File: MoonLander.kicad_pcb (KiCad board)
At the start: 2 copper layers, 37.8 x 22.7 mm, 46 parts, among them IC1 MCP73831/2, IC2 BU33SD5, IC3 PRTR5V0U2X, IC4 CP2110-GM, IC5 LPC824M201JHI33, J1 Cortex_JTAG/SWD_10, P1 CONN_01X02, P2 CONN_01X02, P3 USB_OTG, P4 CONN_02X08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

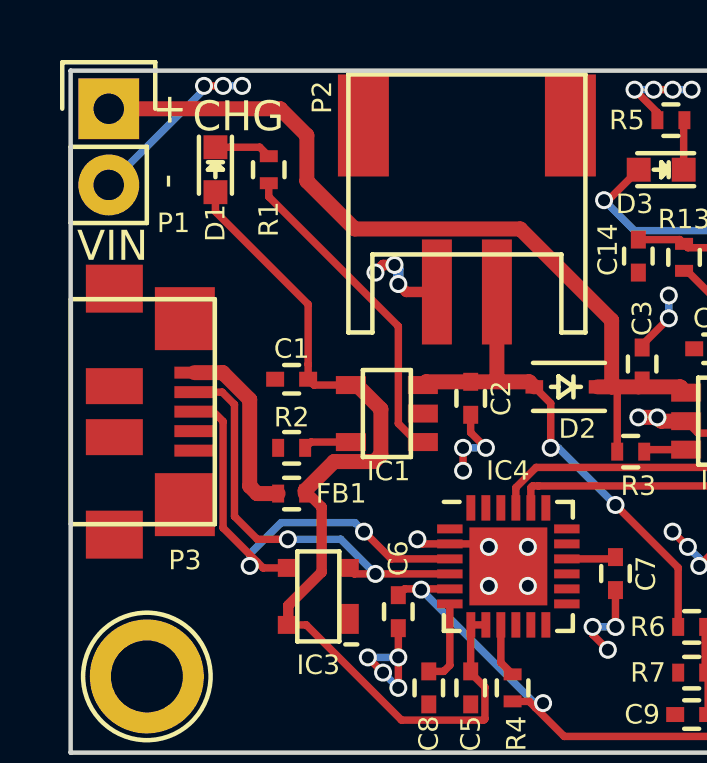
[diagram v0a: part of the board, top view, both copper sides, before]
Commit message: fixed reversed USB pinout
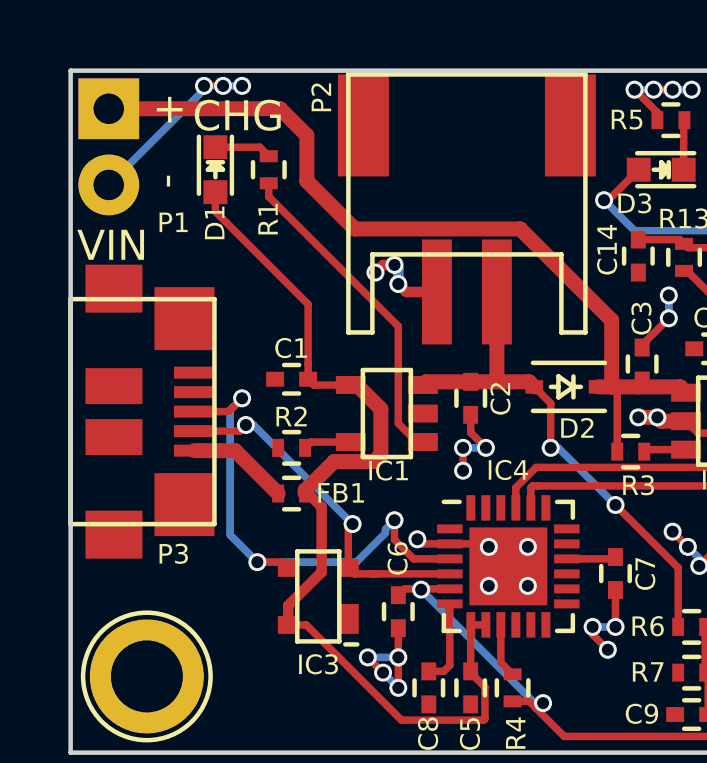
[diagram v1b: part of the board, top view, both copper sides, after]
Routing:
- net Net-(FB1-Pad2): track 6.15 -> 3.39 mm
- net /USB-Serial/USB_D-: track 14.2 -> 11.7 mm
- net /USB-Serial/USB_D+: track 15.7 -> 16.9 mm, vias 2 -> 3

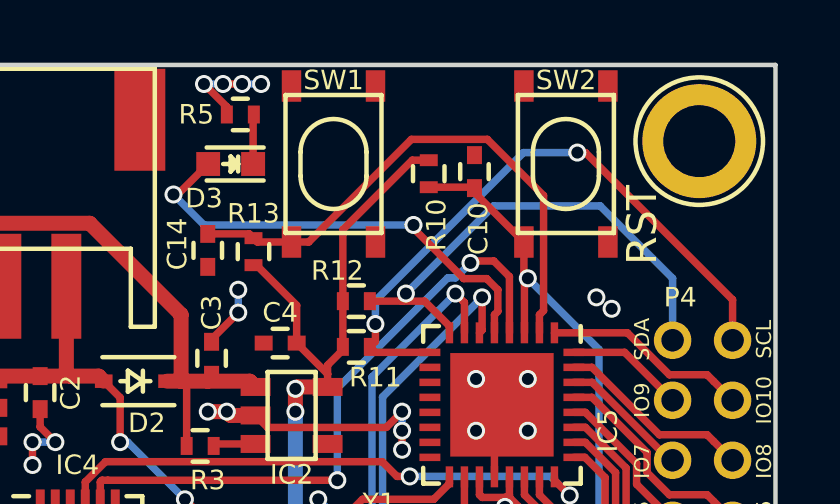
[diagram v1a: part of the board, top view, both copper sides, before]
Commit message: fixed switch footprint and pinout
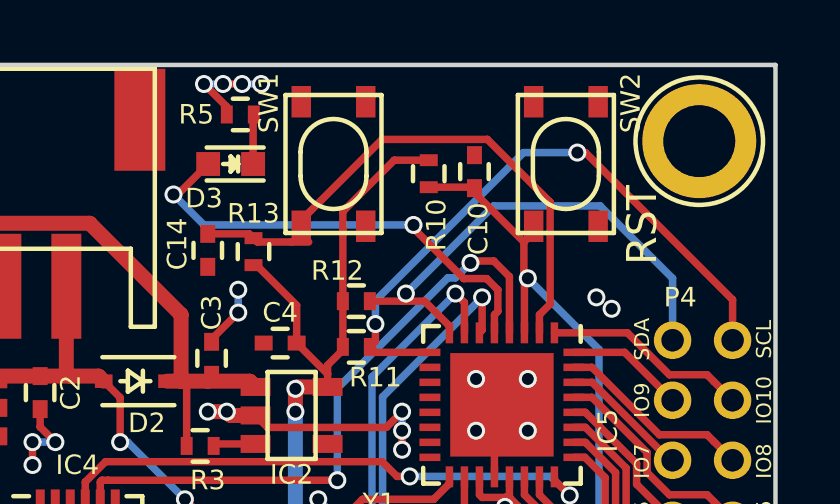
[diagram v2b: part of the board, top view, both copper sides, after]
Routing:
- net /CPU/RESET: track 21.2 -> 21.9 mm

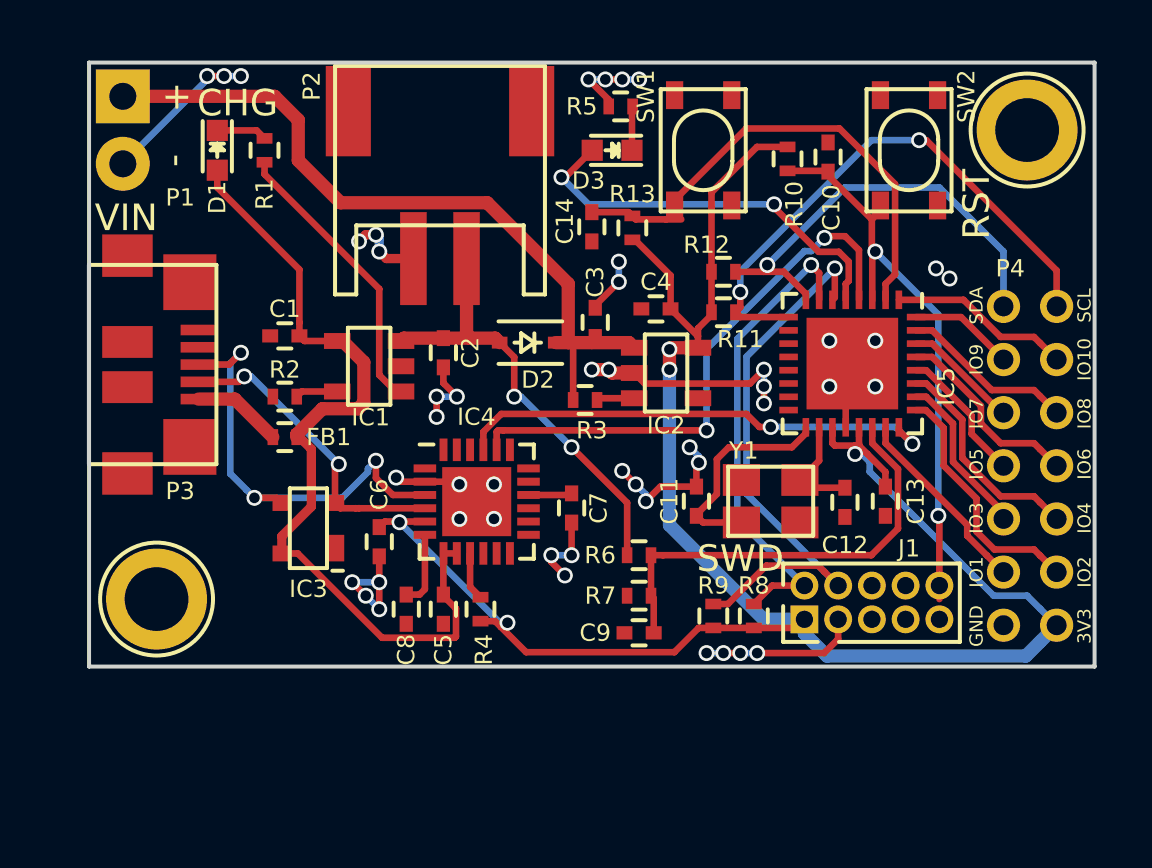
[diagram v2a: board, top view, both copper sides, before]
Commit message: bypass battery if USB connected
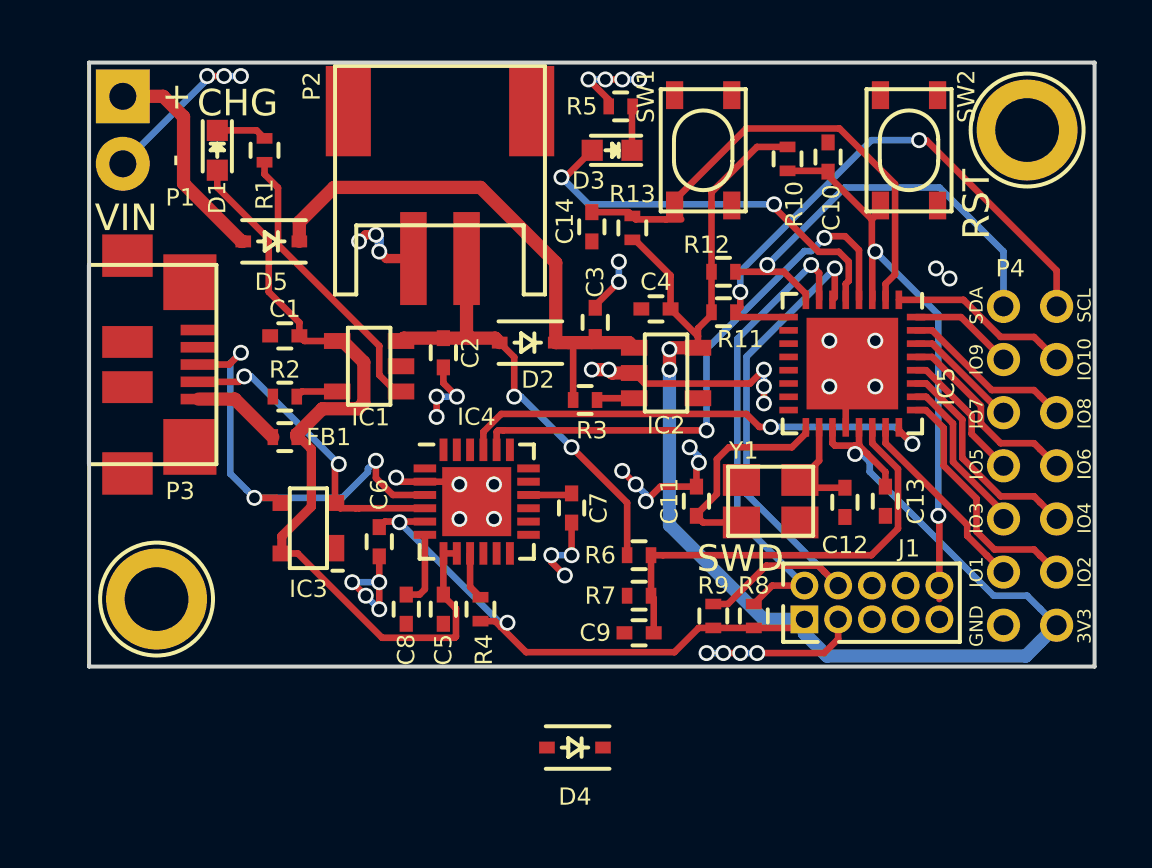
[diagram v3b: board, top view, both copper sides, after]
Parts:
- added D4: D_Schottky, Diodes_SMD:SOD-323, F.Cu at (147.6, 112.5)
- added D5: D_Schottky, Diodes_SMD:SOD-323, F.Cu at (136.1, 93.5)
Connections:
- C3 pad 1: /PowerSupply/V_EXT -> Net-(C3-Pad1)
- D2 pad 1: /PowerSupply/V_EXT -> Net-(C3-Pad1)
- IC2 pad 1: /PowerSupply/V_EXT -> Net-(C3-Pad1)
- R3 pad 2: /PowerSupply/V_EXT -> Net-(C3-Pad1)
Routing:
- net Net-(C3-Pad1): track 0.00 -> 20.6 mm
- net /PowerSupply/V_EXT: track 28.3 -> 8.27 mm

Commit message: switched microUSB footprint, rerouted with new schottkys
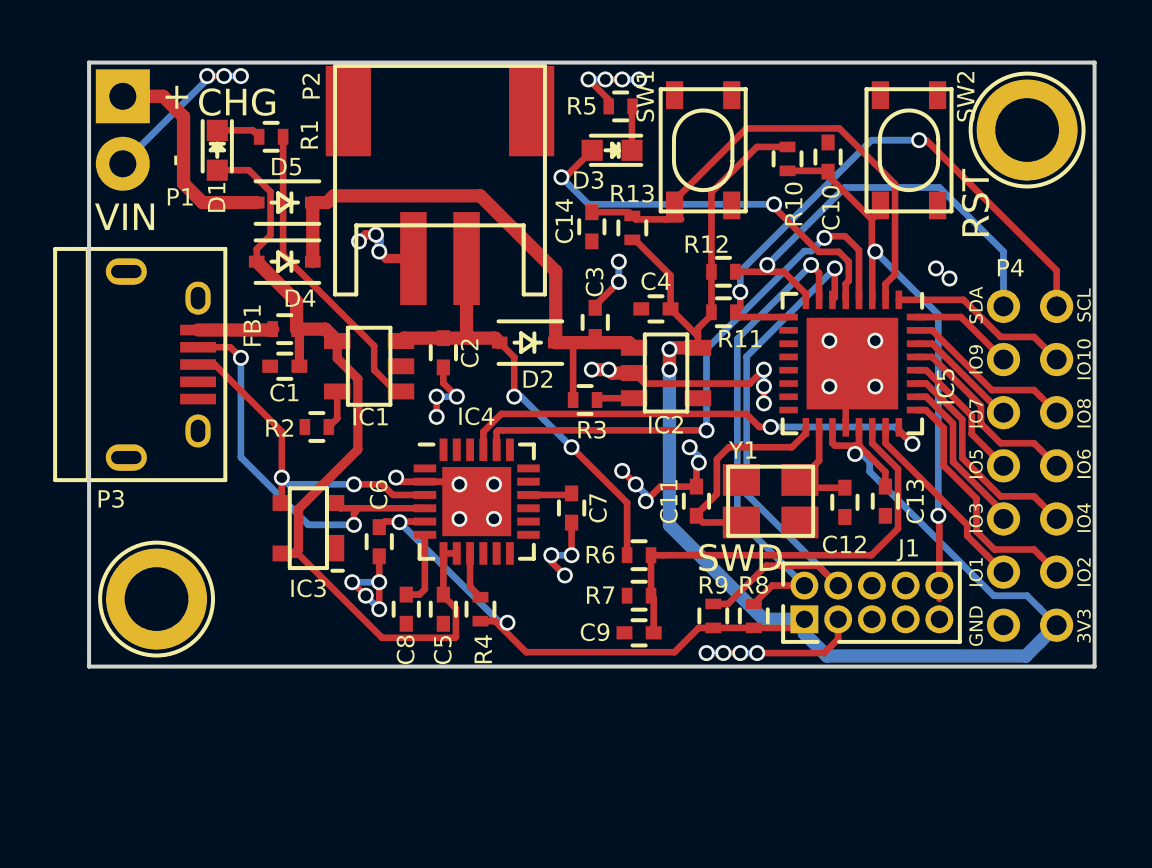
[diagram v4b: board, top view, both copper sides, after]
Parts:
- P3: footprint GrayCatLabs:ZX62R-B-5P -> Connect:USB_Micro-B
- moved D4 21.3 mm to (136.7, 94.2)
- moved FB1 4.06 mm to (136.6, 96.8)
- moved R2 1.66 mm to (137.9, 100.5)
- moved D5 1.55 mm to (136.7, 92.0)
- moved P3 1.35 mm to (131.8, 98.1), turned to 270 degrees
- moved C1 1.14 mm to (136.7, 98.2)
- moved R1 0.57 mm to (136.1, 89.5), turned to 180 degrees
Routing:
- net /USB-Serial/USB_D+: track 16.9 -> 12.5 mm, vias 3 -> 2
- net /USB-Serial/USB_D-: track 11.7 -> 14.9 mm
- net 5V_USB: track 31.9 -> 32.8 mm
- net Net-(IC1-Pad1): track 10.9 -> 11.5 mm
- net Net-(FB1-Pad2): track 3.39 -> 2.82 mm

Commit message: use STITCH_VIA footprint for via stitching
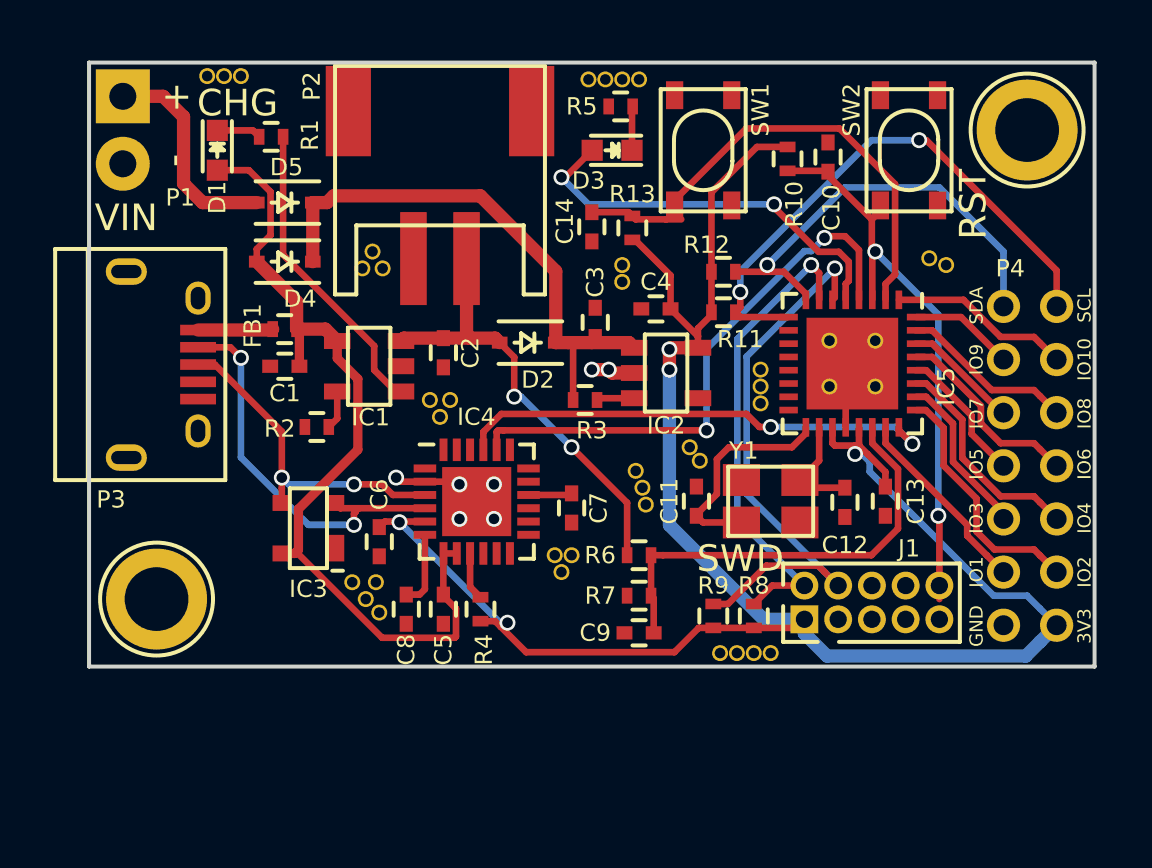
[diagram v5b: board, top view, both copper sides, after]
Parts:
- added REF**: STITCH_VIA, GrayCatLabs:STITCH_VIA, F.Cu at (139.6, 94.5)
- added REF**: STITCH_VIA, GrayCatLabs:STITCH_VIA, F.Cu at (139.2, 106.3)
- added REF**: STITCH_VIA, GrayCatLabs:STITCH_VIA, F.Cu at (147.1, 105.9)
- added REF**: STITCH_VIA, GrayCatLabs:STITCH_VIA, F.Cu at (147.4, 105.3)
- added REF**: STITCH_VIA, GrayCatLabs:STITCH_VIA, F.Cu at (146.8, 105.3)
- added REF**: STITCH_VIA, GrayCatLabs:STITCH_VIA, F.Cu at (153.0, 109.0)
- added REF**: STITCH_VIA, GrayCatLabs:STITCH_VIA, F.Cu at (153.7, 109.0)
- added REF**: STITCH_VIA, GrayCatLabs:STITCH_VIA, F.Cu at (154.3, 109.0)
- added REF**: STITCH_VIA, GrayCatLabs:STITCH_VIA, F.Cu at (154.9, 109.0)
- added REF**: STITCH_VIA, GrayCatLabs:STITCH_VIA, F.Cu at (152.3, 101.7)
- added REF**: STITCH_VIA, GrayCatLabs:STITCH_VIA, F.Cu at (151.9, 101.2)
- added REF**: STITCH_VIA, GrayCatLabs:STITCH_VIA, F.Cu at (140.3, 94.5)
- added REF**: STITCH_VIA, GrayCatLabs:STITCH_VIA, F.Cu at (150.2, 103.4)
- added REF**: STITCH_VIA, GrayCatLabs:STITCH_VIA, F.Cu at (150.1, 102.7)
- added REF**: STITCH_VIA, GrayCatLabs:STITCH_VIA, F.Cu at (149.9, 102.1)
- added REF**: STITCH_VIA, GrayCatLabs:STITCH_VIA, F.Cu at (154.6, 99.6)
- added REF**: STITCH_VIA, GrayCatLabs:STITCH_VIA, F.Cu at (154.6, 98.9)
- added REF**: STITCH_VIA, GrayCatLabs:STITCH_VIA, F.Cu at (154.6, 98.3)
- added REF**: STITCH_VIA, GrayCatLabs:STITCH_VIA, F.Cu at (158.9, 98.9)
- added REF**: STITCH_VIA, GrayCatLabs:STITCH_VIA, F.Cu at (157.2, 98.9)
- added REF**: STITCH_VIA, GrayCatLabs:STITCH_VIA, F.Cu at (157.2, 97.2)
- added REF**: STITCH_VIA, GrayCatLabs:STITCH_VIA, F.Cu at (158.9, 97.2)
- added REF**: STITCH_VIA, GrayCatLabs:STITCH_VIA, F.Cu at (140.0, 93.9)
- added REF**: STITCH_VIA, GrayCatLabs:STITCH_VIA, F.Cu at (161.5, 94.4)
- added REF**: STITCH_VIA, GrayCatLabs:STITCH_VIA, F.Cu at (160.9, 94.1)
- added REF**: STITCH_VIA, GrayCatLabs:STITCH_VIA, F.Cu at (149.4, 95.0)
- added REF**: STITCH_VIA, GrayCatLabs:STITCH_VIA, F.Cu at (149.4, 94.4)
- added REF**: STITCH_VIA, GrayCatLabs:STITCH_VIA, F.Cu at (150.0, 87.4)
- added REF**: STITCH_VIA, GrayCatLabs:STITCH_VIA, F.Cu at (149.4, 87.4)
- added REF**: STITCH_VIA, GrayCatLabs:STITCH_VIA, F.Cu at (148.7, 87.4)
- added REF**: STITCH_VIA, GrayCatLabs:STITCH_VIA, F.Cu at (148.1, 87.4)
- added REF**: STITCH_VIA, GrayCatLabs:STITCH_VIA, F.Cu at (135.0, 87.2)
- added REF**: STITCH_VIA, GrayCatLabs:STITCH_VIA, F.Cu at (134.4, 87.2)
- added REF**: STITCH_VIA, GrayCatLabs:STITCH_VIA, F.Cu at (142.5, 100.1)
- added REF**: STITCH_VIA, GrayCatLabs:STITCH_VIA, F.Cu at (133.7, 87.2)
- added REF**: STITCH_VIA, GrayCatLabs:STITCH_VIA, F.Cu at (142.9, 99.4)
- added REF**: STITCH_VIA, GrayCatLabs:STITCH_VIA, F.Cu at (142.1, 99.4)
- added REF**: STITCH_VIA, GrayCatLabs:STITCH_VIA, F.Cu at (140.2, 107.4)
- added REF**: STITCH_VIA, GrayCatLabs:STITCH_VIA, F.Cu at (139.7, 106.9)
- added REF**: STITCH_VIA, GrayCatLabs:STITCH_VIA, F.Cu at (140.1, 106.3)
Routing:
- net GND: track 48.0 -> 5.14 mm, vias 45 -> 7
- net (no net): vias 2 -> 0

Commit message: added some silk
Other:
- board text added: "Gray Cat Labs"
- board text added: "MoonLander RevB"
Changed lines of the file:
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@@
-(kicad_pcb (version 4) (host pcbnew 0.201601081511+6431~40~ubuntu15.10.1-stable)
+(kicad_pcb (version 4) (host pcbnew 0.201601091448+6432~40~ubuntu15.10.1-stable)
   (general
-    (links 0)
-    (no_connects 10)
+    (links 167)
+    (no_connects 0)
     (area 129.210999 86.665999 167.207001 109.549001)
     (thickness 1.6)
-    (drawings 36)
+    (drawings 38)
     (tracks 384)
     (zones 0)
@@
   )
   (setup
-    (last_trace_width 0.5)
+    (last_trace_width 0.25)
     (user_trace_width 0.1524)
     (user_trace_width 0.2)
@@
       (net 2 GND) (zone_connect 2))
   )
+  (gr_text "Gray Cat Labs" (at 149.733 92.075) (layer B.SilkS)
+    (effects (font (size 1.25 1.25) (thickness 0.2)) (justify left mirror))
+  )
+  (gr_text "MoonLander RevB" (at 149.733 89.916) (layer B.SilkS)
+    (effects (font (size 1.25 1.25) (thickness 0.2)) (justify left mirror))
+  )
   (gr_text SCL (at 166.751 95.885 90) (layer F.SilkS)
